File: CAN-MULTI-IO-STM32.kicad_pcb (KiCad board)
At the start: 2 copper layers, 81 x 55 mm, 66 parts, among them J1 H GND L, J2 TERM, J3 USART1, J5 PWR IN, U1 STM32L433RCT3, U2 MCP2562-E-SN, U3 LMR54410, U4 ADS1015IDGS, U5 PCA9537, U6 PI6ULS5V9511AUEX

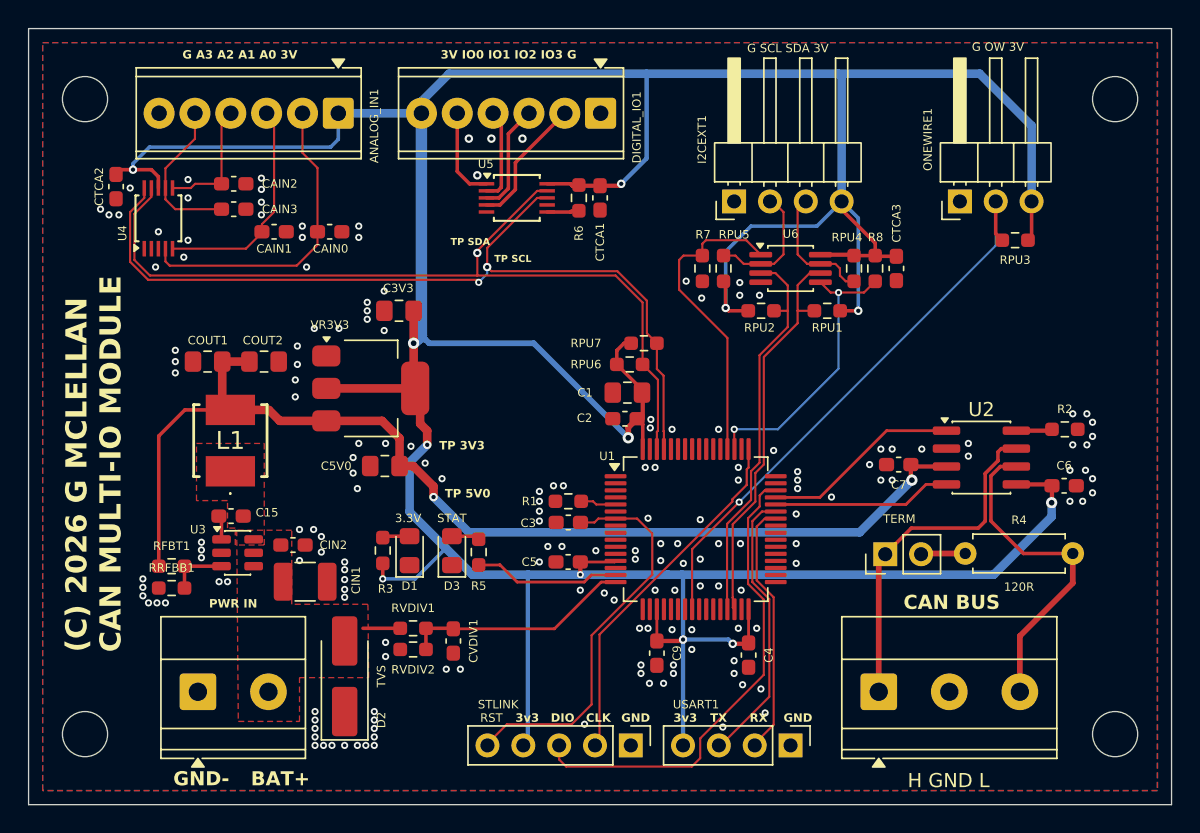
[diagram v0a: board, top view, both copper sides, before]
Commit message: switch to STM32G0B1 micro, refactor pcb layout
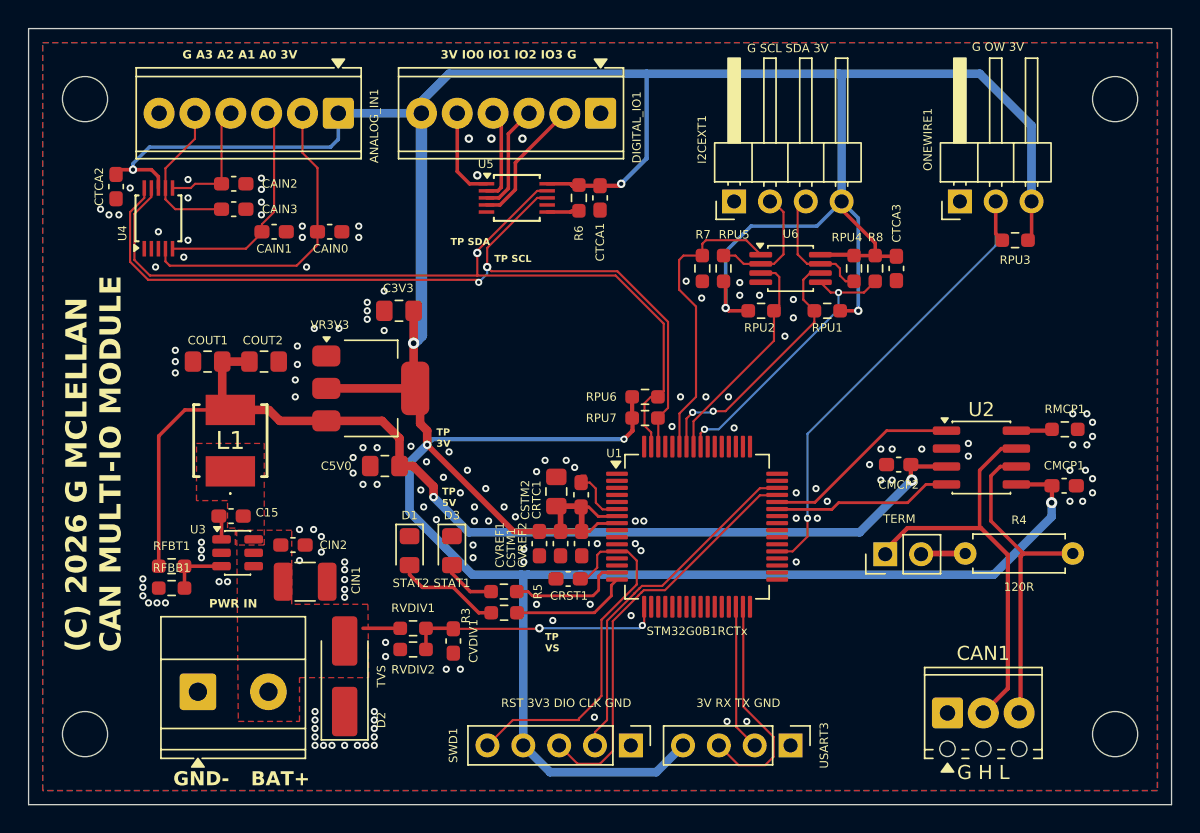
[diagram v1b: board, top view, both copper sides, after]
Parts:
- removed R1: 10K, Resistor_SMD:R_0603_1608Metric_Pad0.98x0.95mm_HandSolder
- CAN1: renamed from J1; value H GND L -> G H L; footprint TerminalBlock_Phoenix:TerminalBlock_Phoenix_MKDS-1,5-3_1x03_P5.00mm_Horizontal -> TerminalBlock_Phoenix:TerminalBlock_Phoenix_MPT-0,5-3-2.54_1x03_P2.54mm_Horizontal
- D1: value 3.3V -> STAT2
- D3: value STAT -> STAT1
- SWD1: value STLINK -> RST 3V3 DIO CLK GND
- U1: value STM32L433RCT3 -> STM32G0B1RCTx
- USART3: renamed from J3; value USART1 -> 3V RX TX GND
- moved CRTC1 16.4 mm to (136.2, 108.0), turned to 90 degrees
- moved CVREF1 10.7 mm to (133.2, 111.5), turned to -90 degrees
- moved R3 9.67 mm to (130.7, 116.4), turned to 0 degrees
- moved CVREF2 9.41 mm to (136.2, 111.5)
- moved CSTM2 8.63 mm to (134.4, 107.8), turned to 90 degrees
- moved RPU7 5.30 mm to (140.7, 102.6)
- moved CAN1 5.10 mm to (162.1, 123.5)
- moved CRST1 4.00 mm to (135.2, 114.0)
- moved R5 3.32 mm to (130.7, 114.9), turned to 0 degrees
- moved RPU6 2.54 mm to (140.7, 101.1)
- moved CSTM1 1.41 mm to (134.7, 111.5), turned to -90 degrees
- moved U1 0.20 mm to (144.4, 110.3)
- turned D1 to -90 degrees
- turned D3 to -90 degrees
- renumbered C6 to CMCP1, C7 to CMCP2, C3 to CRST1, C4 to CRTC1, C5 to CSTM1, C1 to CSTM2, C2 to CVREF1, C9 to CVREF2, RRFBB1 to RFBB1, R2 to RMCP1
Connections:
- net /STATUS renamed /STAT1
- CAN1 pad 1: /CANH -> GND
- CAN1 pad 2: GND -> /CANH
- CRTC1 pad 2: GND -> /VRTC
- R3 pad 1: +3.3V -> Net-(D1-A)
- R3 pad 2: Net-(D1-A) -> /STAT2
- U1 pad 12: GND -> /NRST
- U1 pad 13: +3.3V -> unconnected-(U1-PC0-Pad13)
- U1 pad 16: /VDIV -> /STAT2
- U1 pad 17: unconnected-(U1-PA3-Pad17) -> /VDIV
- U1 pad 18: GND -> unconnected-(U1-PA1-Pad18)
- U1 pad 19: +3.3V -> unconnected-(U1-PA2-Pad19)
- U1 pad 24: /ONEW -> unconnected-(U1-PA7-Pad24)
- U1 pad 29: /I2C2_SCL -> unconnected-(U1-PB2-Pad29)
- U1 pad 30: /I2C2_SDA -> /USART3_TX
- U1 pad 31: GND -> /USART3_RX
- U1 pad 32: +3.3V -> unconnected-(U1-PB12-Pad32)
- U1 pad 37: unconnected-(U1-PC6-Pad37) -> /ONEW
- U1 pad 42: /USART1_TX -> unconnected-(U1-PA10/UCPD1_DBCC2-Pad42)
- U1 pad 43: /USART1_RX -> /CAN1_RX
- U1 pad 44: /CAN1_RX -> /CAN1_TX
- U1 pad 45: /CAN1_TX -> /SWDIO
- U1 pad 46: /SWDIO -> /SWCLK
- U1 pad 47: GND -> unconnected-(U1-PA15-Pad47)
- U1 pad 48: GND -> unconnected-(U1-PC8-Pad48)
- U1 pad 49: /SWCLK -> unconnected-(U1-PC9-Pad49)
- U1 pad 5: /BOOT0 -> unconnected-(U1-PC15-Pad5)
- U1 pad 51: /TCA_RDY -> unconnected-(U1-PD1-Pad51)
- U1 pad 52: /TCA_EN -> unconnected-(U1-PD2-Pad52)
- U1 pad 56: unconnected-(U1-PB4-Pad56) -> /TCA_RDY
- U1 pad 57: unconnected-(U1-PB5-Pad57) -> /I2C2_SCL
- U1 pad 58: unconnected-(U1-PB6-Pad58) -> /I2C2_SDA
- U1 pad 59: unconnected-(U1-PB7-Pad59) -> /TCA_EN
- U1 pad 6: unconnected-(U1-PH1-Pad6) -> /VRTC
- U1 pad 61: /I2C1_SCL -> unconnected-(U1-PB7-Pad61)
- U1 pad 62: /I2C1_SDA -> /I2C1_SCL
- U1 pad 63: GND -> /I2C1_SDA
- U1 pad 64: +3.3V -> unconnected-(U1-PC10-Pad64)
- U1 pad 7: /NRST -> +3.3V
- U1 pad 8: unconnected-(U1-PC0-Pad8) -> +3.3V
- U1 pad 9: unconnected-(U1-PC1-Pad9) -> GND
- USART3 pad 2: /USART1_TX -> /USART3_TX
- USART3 pad 3: /USART1_RX -> /USART3_RX
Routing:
- net /USART1_RX: track 19.9 -> 0.00 mm
- net /USART1_TX: track 18.0 -> 0.00 mm
- net /USART3_RX: track 0.00 -> 16.2 mm
- net /I2C2_SCL: track 28.0 -> 16.0 mm
- net /USART3_TX: track 0.00 -> 10.3 mm
- net /I2C2_SDA: track 28.1 -> 18.6 mm, vias 0 -> 2
- net /STAT2: track 0.00 -> 8.50 mm
- net +3.3V: track 304.2 -> 297.6 mm, vias 12 -> 8
- net /ONEW: track 40.8 -> 34.8 mm
- net Net-(D1-A): track 1.80 -> 7.58 mm
- net /CANH: track 24.0 -> 29.7 mm
- net /SWDIO: track 34.0 -> 29.3 mm
- net /VRTC: track 0.00 -> 4.11 mm
- net /BOOT0: track 2.53 -> 0.00 mm
- net Net-(D3-A): track 1.69 -> 3.89 mm
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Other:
- board text added: "TP 3V"
- board text added: "TP 5V"
- board text added: "TP VS"
- board text removed: "3v3"
- board text removed: "CAN BUS"
- board text removed: "CLK"
- board text removed: "DIO"
- board text removed: "GND"
- board text removed: "RST"
- board text removed: "RX"
- board text removed: "TP 3V3"
- board text removed: "TP 5V0"
- board text removed: "TX"

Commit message: added ground stitching, silkscreen tweaks, refined 3v supply for STM
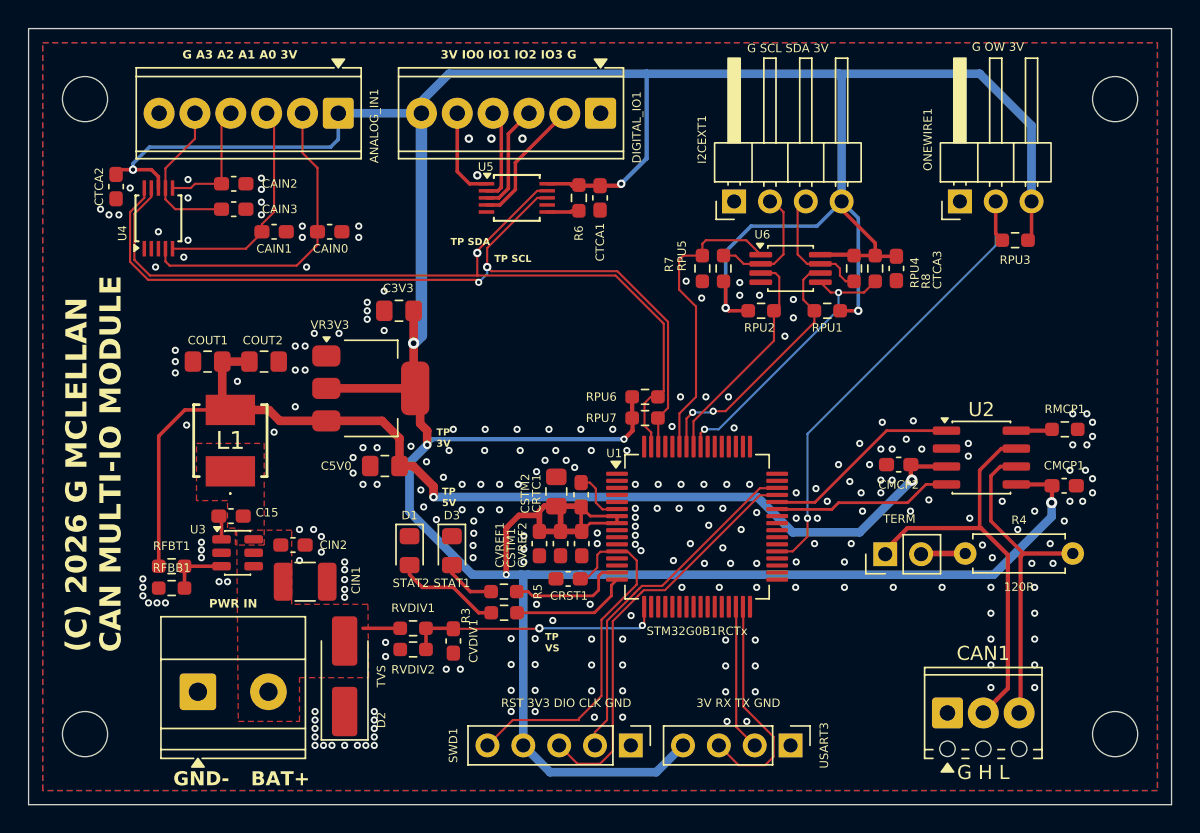
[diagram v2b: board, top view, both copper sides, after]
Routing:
- net +3.3V: track 297.6 -> 296.1 mm, vias 8 -> 9
- net /I2C2_SDA: track 18.6 -> 17.9 mm
- net GND: vias 157 -> 258
